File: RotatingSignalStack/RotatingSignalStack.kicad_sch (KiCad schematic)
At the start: 0 parts

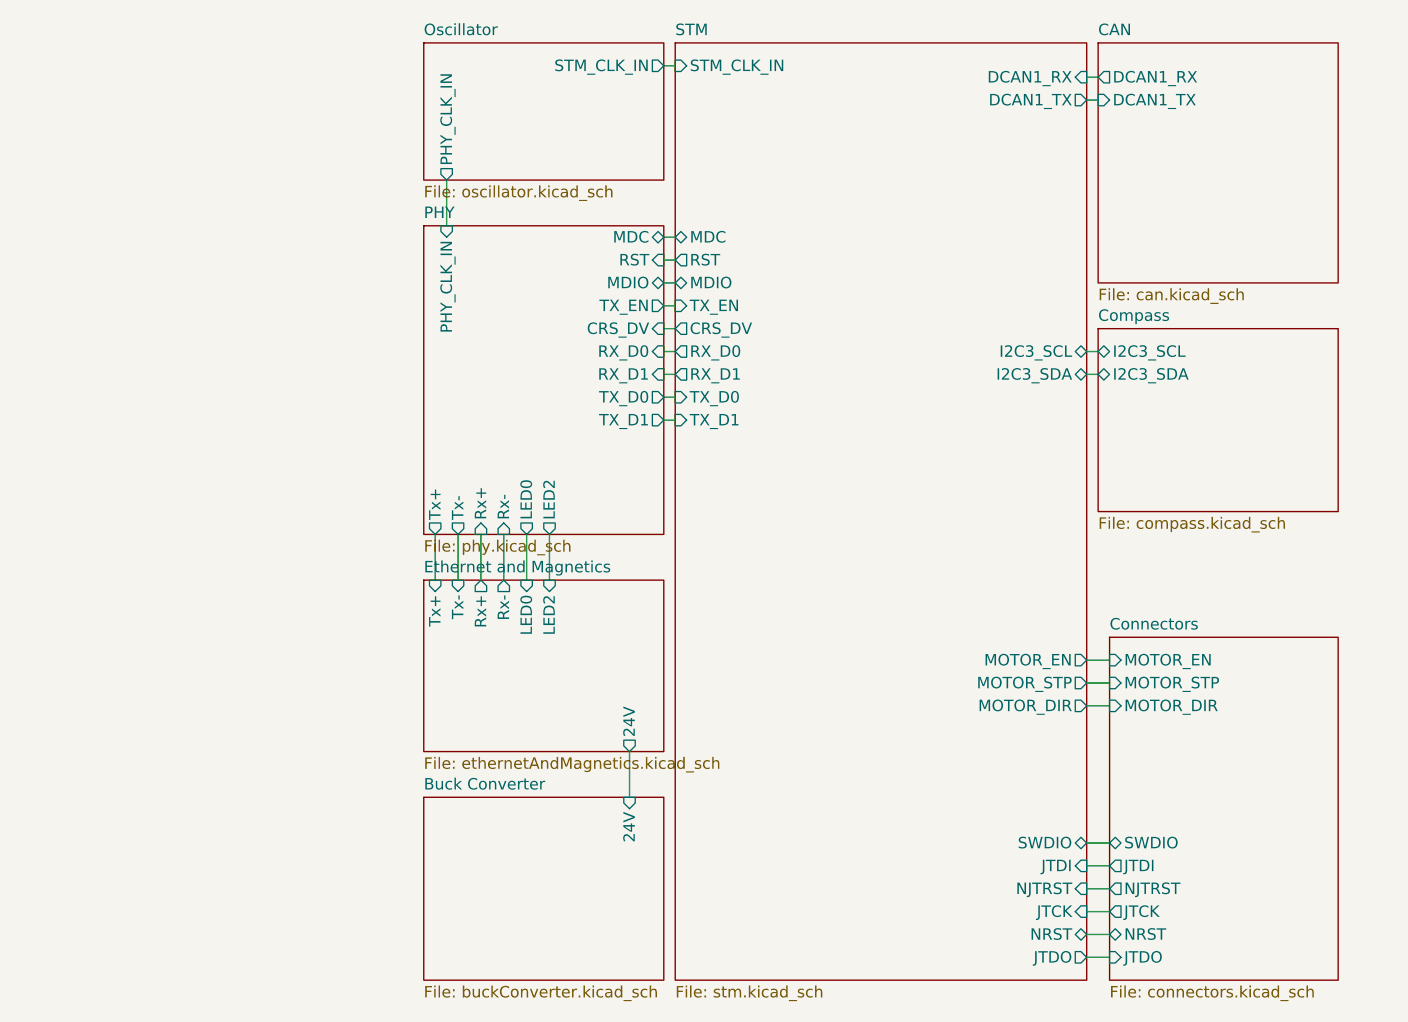
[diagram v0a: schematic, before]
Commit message: Added Motor connector CAN
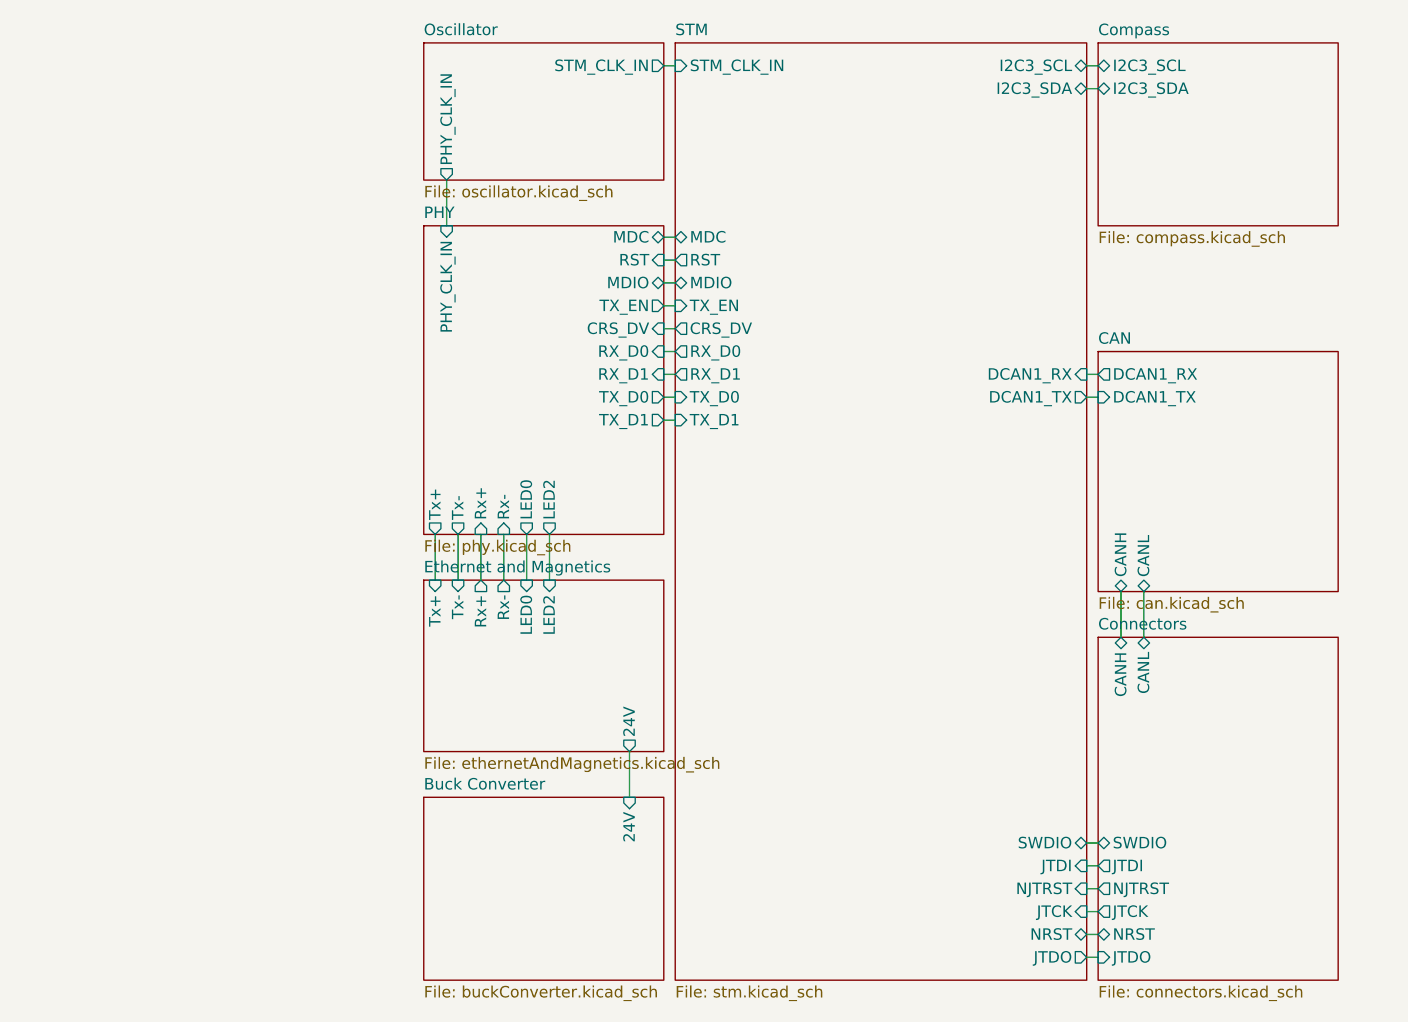
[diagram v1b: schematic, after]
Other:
- sheet CAN ports: added CANH, CANL; removed none
- sheet Connectors ports: added CANH, CANL; removed MOTOR_DIR, MOTOR_EN, MOTOR_STP
- sheet STM ports: added none; removed MOTOR_DIR, MOTOR_EN, MOTOR_STP

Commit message: Added buttons
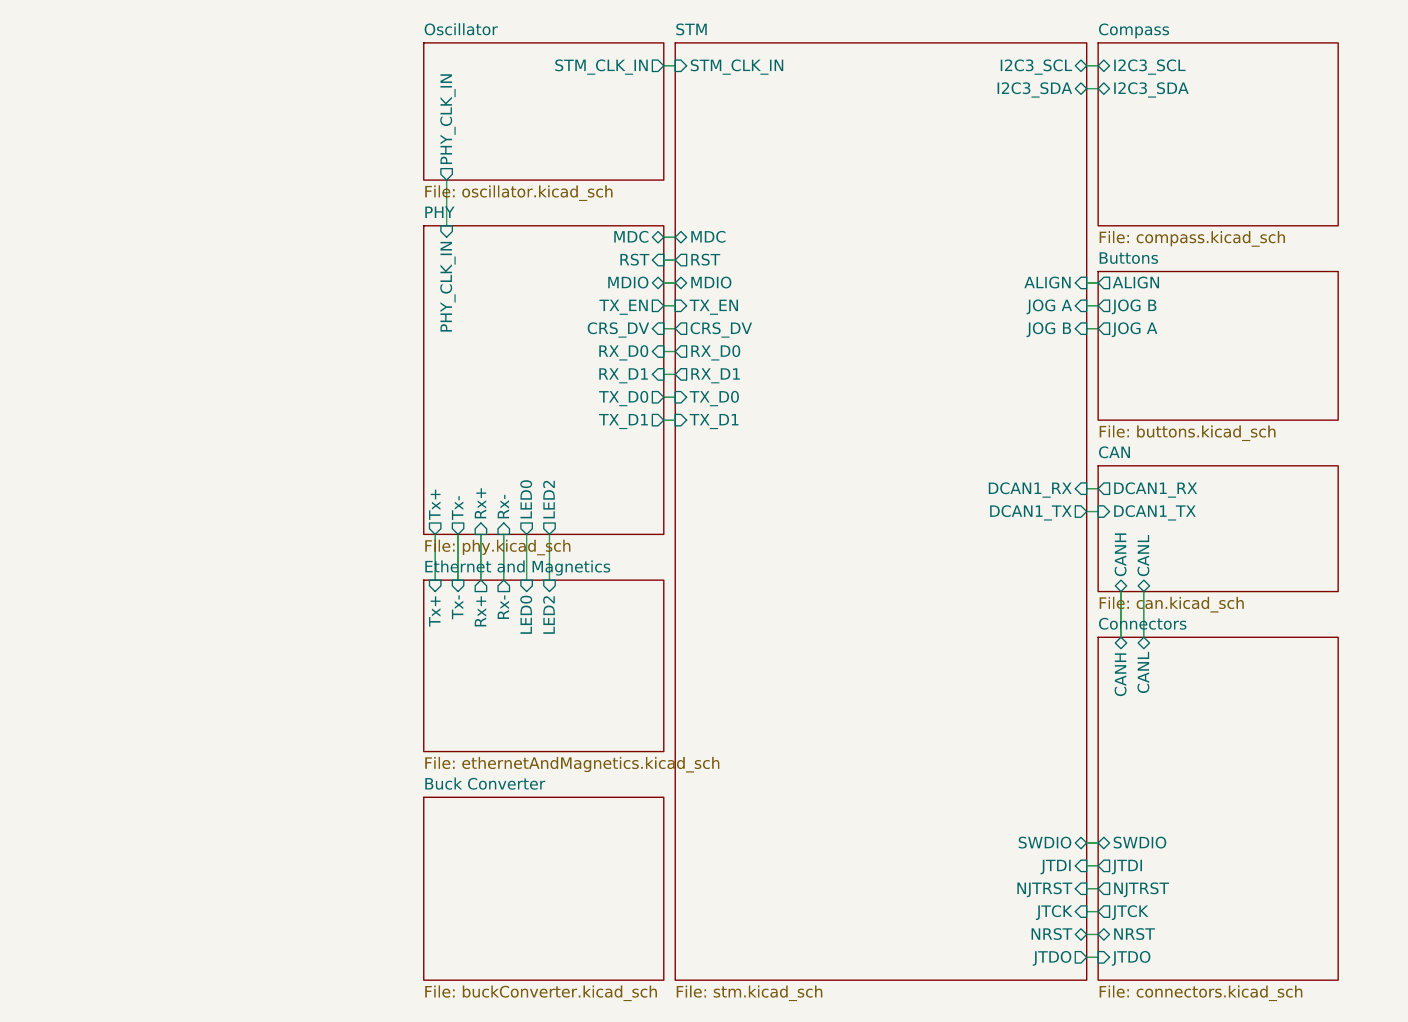
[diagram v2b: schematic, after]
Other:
- added sheet Buttons (buttons.kicad_sch)
- sheet Buck Converter ports: added none; removed 24V
- sheet Ethernet and Magnetics ports: added none; removed 24V
- sheet STM ports: added ALIGN, JOG A, JOG B; removed none
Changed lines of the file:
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@@
-	(wire
-		(pts
-			(xy 173.99 72.39) (xy 175.26 72.39)
-		)
-		(stroke
-			(width 0)
-			(type default)
-		)
-	)
 	(wire
 		(pts
@@
 	(wire
 		(pts
+			(xy 173.99 62.23) (xy 175.26 62.23)
+		)
+		(stroke
+			(width 0)
+			(type default)
+		)
+	)
+	(wire
+		(pts
 			(xy 173.99 134.62) (xy 175.26 134.62)
 		)
@@
 	(wire
 		(pts
+			(xy 173.99 64.77) (xy 175.26 64.77)
+		)
+		(stroke
+			(width 0)
+			(type default)
+		)
+	)
+	(wire
+		(pts
 			(xy 106.68 87.63) (xy 106.68 92.71)
 		)
@@
 	(wire
 		(pts
+			(xy 173.99 85.09) (xy 175.26 85.09)
+		)
+		(stroke
+			(width 0)
+			(type default)
+		)
+	)
+	(wire
+		(pts
 			(xy 127 35.56) (xy 128.27 35.56)
 		)
@@
 	(wire
 		(pts
-			(xy 123.19 111.76) (xy 123.19 116.84)
-		)
-		(stroke
-			(width 0)
-			(type default)
-		)
-	)
-	(wire
-		(pts
 			(xy 127 64.77) (xy 128.27 64.77)
 		)
@@
 	(wire
 		(pts
+			(xy 173.99 59.69) (xy 175.26 59.69)
+		)
+		(stroke
+			(width 0)
+			(type default)
+		)
+	)
+	(wire
+		(pts
 			(xy 177.8 93.98) (xy 177.8 99.06)
 		)
@@
 	(wire
 		(pts
+			(xy 173.99 82.55) (xy 175.26 82.55)
+		)
+		(stroke
+			(width 0)
+			(type default)
+		)
+	)
+	(wire
+		(pts
 			(xy 101.6 87.63) (xy 101.6 92.71)
 		)
@@
 		(pts
 			(xy 173.99 129.54) (xy 175.26 129.54)
-		)
-		(stroke
-			(width 0)
-			(type default)
-		)
-	)
-	(wire
-		(pts
-			(xy 173.99 69.85) (xy 175.26 69.85)
 		)
 		(stroke
@@
 			)
 		)
-		(pin "24V" output
-			(at 123.19 111.76 270)
-			(effects
-				(font
-					(size 1.27 1.27)
-				)
-				(justify left)
-			)
-		)
 		(instances
 			(project "RotatingSignalStack"
@@
 		)
 		(pin "DCAN1_RX" input
-			(at 173.99 69.85 0)
+			(at 173.99 82.55 0)
 			(effects
 				(font
@@
 		)
 		(pin "DCAN1_TX" output
-			(at 173.99 72.39 0)
+			(at 173.99 85.09 0)
 			(effects
 				(font
@@
 		(pin "SWDIO" bidirectional
 			(at 173.99 121.92 0)
+			(effects
+				(font
+					(size 1.27 1.27)
+				)
+				(justify right)
+			)
+		)
+		(pin "JOG B" input
+			(at 173.99 64.77 0)
+			(effects
+				(font
+					(size 1.27 1.27)
+				)
+				(justify right)
+			)
+		)
+		(pin "JOG A" input
+			(at 173.99 62.23 0)
+			(effects
+				(font
+					(size 1.27 1.27)
+				)
+				(justify right)
+			)
+		)
+		(pin "ALIGN" input
+			(at 173.99 59.69 0)
 			(effects
 				(font
@@
 	)
 	(sheet
-		(at 175.26 67.31)
-		(size 26.67 26.67)
+		(at 175.26 58.42)
+		(size 26.67 16.51)
 		(exclude_from_sim no)
 		(in_bom yes)
@@
 			(color 0 0 0 0.0000)
 		)
+		(property "Sheetname" "Buttons"
+			(at 175.26 57.7084 0)
+			(effects
+				(font
+					(size 1.27 1.27)
+				)
+				(justify left bottom)
+			)
+		)
+		(property "Sheetfile" "buttons.kicad_sch"
+			(at 175.26 75.5146 0)
+			(effects
+				(font
+					(size 1.27 1.27)
+				)
+				(justify left top)
+			)
+		)
+		(pin "ALIGN" output
+			(at 175.26 59.69 180)
+			(effects
+				(font
+					(size 1.27 1.27)
+				)
+				(justify left)
+			)
+		)
+		(pin "JOG B" output
+			(at 175.26 62.23 180)
+			(effects
+				(font
+					(size 1.27 1.27)
+				)
+				(justify left)
+			)
+		)
+		(pin "JOG A" output
+			(at 175.26 64.77 180)
+			(effects
+				(font
+					(size 1.27 1.27)
+				)
+				(justify left)
+			)
+		)
+		(instances
+			(project "RotatingSignalStack"
+				(path "/fbbbfa89-3c28-4cf8-856b-66ca7308742c"
+					(page "10")
+				)
+			)
+		)
+	)
+	(sheet
+		(at 175.26 80.01)
+		(size 26.67 13.97)
+		(exclude_from_sim no)
+		(in_bom yes)
+		(on_board yes)
+		(dnp no)
+		(fields_autoplaced yes)
+		(stroke
+			(width 0.1524)
+			(type solid)
+		)
+		(fill
+			(color 0 0 0 0.0000)
+		)
 		(property "Sheetname" "CAN"
-			(at 175.26 66.5984 0)
+			(at 175.26 79.2984 0)
 			(effects
 				(font
@@
 		)
 		(pin "DCAN1_RX" output
-			(at 175.26 69.85 180)
+			(at 175.26 82.55 180)
 			(effects
 				(font
@@
 		)
 		(pin "DCAN1_TX" input
-			(at 175.26 72.39 180)
+			(at 175.26 85.09 180)
 			(effects
 				(font
@@
 			)
 		)
-		(pin "24V" input
-			(at 123.19 116.84 90)
-			(effects
-				(font
-					(size 1.27 1.27)
-				)
-				(justify right)
-			)
-		)

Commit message: Added everything
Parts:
- added H1, H2, H3, H4: MountingHole, MRDT_Drill_Holes:4_40_Hole_Corner, symbol Mechanical:MountingHole
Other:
- sheet Connectors ports: added SWDCLK, SWO; removed JTCK, JTDI, JTDO, NJTRST
- sheet STM ports: added SWCLK, SWO; removed JTCK, JTDI, JTDO, NJTRST

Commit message: placement fix
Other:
- removed sheet Connectors
- sheet CAN ports: added none; removed CANH, CANL
- sheet STM ports: added none; removed NRST, SWCLK, SWDIO, SWO
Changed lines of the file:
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@@
-	(wire
-		(pts
-			(xy 180.34 93.98) (xy 180.34 99.06)
-		)
-		(stroke
-			(width 0)
-			(type default)
-		)
-	)
 	(wire
 		(pts
@@
 	(wire
 		(pts
-			(xy 173.99 129.54) (xy 175.26 129.54)
-		)
-		(stroke
-			(width 0)
-			(type default)
-		)
-	)
-	(wire
-		(pts
 			(xy 173.99 35.56) (xy 175.26 35.56)
 		)
@@
 	(wire
 		(pts
-			(xy 173.99 127) (xy 175.26 127)
-		)
-		(stroke
-			(width 0)
-			(type default)
-		)
-	)
-	(wire
-		(pts
 			(xy 127 64.77) (xy 128.27 64.77)
 		)
@@
 	(wire
 		(pts
-			(xy 177.8 93.98) (xy 177.8 99.06)
-		)
-		(stroke
-			(width 0)
-			(type default)
-		)
-	)
-	(wire
-		(pts
 			(xy 173.99 82.55) (xy 175.26 82.55)
 		)
@@
 	(wire
 		(pts
-			(xy 173.99 134.62) (xy 175.26 134.62)
-		)
-		(stroke
-			(width 0)
-			(type default)
-		)
-	)
-	(wire
-		(pts
 			(xy 127 54.61) (xy 128.27 54.61)
 		)
@@
 		(pts
 			(xy 127 69.85) (xy 128.27 69.85)
-		)
-		(stroke
-			(width 0)
-			(type default)
-		)
-	)
-	(wire
-		(pts
-			(xy 173.99 132.08) (xy 175.26 132.08)
 		)
 		(stroke
@@
 			)
 		)
-		(pin "SWO" output
-			(at 173.99 127 0)
-			(effects
-				(font
-					(size 1.27 1.27)
-				)
-				(justify right)
-			)
-		)
-		(pin "SWCLK" input
-			(at 173.99 129.54 0)
-			(effects
-				(font
-					(size 1.27 1.27)
-				)
-				(justify right)
-			)
-		)
-		(pin "SWDIO" bidirectional
-			(at 173.99 132.08 0)
-			(effects
-				(font
-					(size 1.27 1.27)
-				)
-				(justify right)
-			)
-		)
-		(pin "NRST" bidirectional
-			(at 173.99 134.62 0)
-			(effects
-				(font
-					(size 1.27 1.27)
-				)
-				(justify right)
-			)
-		)
 		(instances
 			(project "RotatingSignalStack"
@@
 			)
 		)
-		(pin "CANH" bidirectional
-			(at 177.8 93.98 270)
-			(effects
-				(font
-					(size 1.27 1.27)
-				)
-				(justify left)
-			)
-		)
-		(pin "CANL" bidirectional
-			(at 180.34 93.98 270)
-			(effects
-				(font
-					(size 1.27 1.27)
-				)
-				(justify left)
-			)
-		)
 		(instances
 			(project "RotatingSignalStack"
@@
 				)
 			)
-		)
-	)
-	(sheet
-		(at 175.26 99.06)
-		(size 26.67 38.1)
-		(exclude_from_sim no)
-		(in_bom yes)
-		(on_board yes)
-		(dnp no)
-		(fields_autoplaced yes)
-		(stroke
-			(width 0.1524)
-			(type solid)
-		)
-		(fill
-			(color 0 0 0 0.0000)
-		)
-		(property "Sheetname" "Connectors"
-			(at 175.26 98.3484 0)
-			(effects
-				(font
-					(size 1.27 1.27)
-				)
-				(justify left bottom)
-			)
-		)
-		(property "Sheetfile" "connectors.kicad_sch"
-			(at 175.26 137.7446 0)
-			(effects
-				(font
-					(size 1.27 1.27)
-				)
-				(justify left top)
-			)
-		)
-		(pin "CANH" bidirectional
-			(at 177.8 99.06 90)
-			(effects
-				(font
-					(size 1.27 1.27)
-				)
-				(justify right)
-			)
-		)
-		(pin "CANL" bidirectional
-			(at 180.34 99.06 90)
-			(effects
-				(font
-					(size 1.27 1.27)
-				)
-				(justify right)
-			)
-		)
-		(pin "NRST" bidirectional
-			(at 175.26 134.62 180)
-			(effects
-				(font
-					(size 1.27 1.27)
-				)
-				(justify left)
-			)
-		)
-		(pin "SWDCLK" output
-			(at 175.26 129.54 180)
-			(effects
-				(font
-					(size 1.27 1.27)
-				)
-				(justify left)
-			)
-		)
-		(pin "SWDIO" bidirectional
-			(at 175.26 132.08 180)
-			(effects
-				(font
-					(size 1.27 1.27)
-				)
-				(justify left)
-			)
-		)
-		(pin "SWO" input
-			(at 175.26 127 180)
-			(effects
-				(font
-					(size 1.27 1.27)
-				)
-				(justify left)
-			)
-		)
-		(instances
-			(project "RotatingSignalStack"
-				(path "/fbbbfa89-3c28-4cf8-856b-66ca7308742c"
-					(page "9")
-				)
-			)

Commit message: Added ground edges and fixed capacitors and layout issues
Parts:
- H1: footprint MRDT_Drill_Holes:4_40_Hole_Corner -> MountingHole:MountingHole_3.2mm_M3_Pad_Via
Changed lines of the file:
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@@
 			)
 		)
-		(property "Footprint" "MRDT_Drill_Holes:4_40_Hole_Corner"
+		(property "Footprint" "MountingHole:MountingHole_3.2mm_M3_Pad_Via"
 			(at 76.2 123.19 0)
 			(effects
